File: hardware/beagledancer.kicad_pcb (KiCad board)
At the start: 2 copper layers, 32 x 23.1 mm, 12 parts, among them J1 USB-MICRO-B, P9 BeagleBone, U1 MAX3421, X1 XTAL4PIN

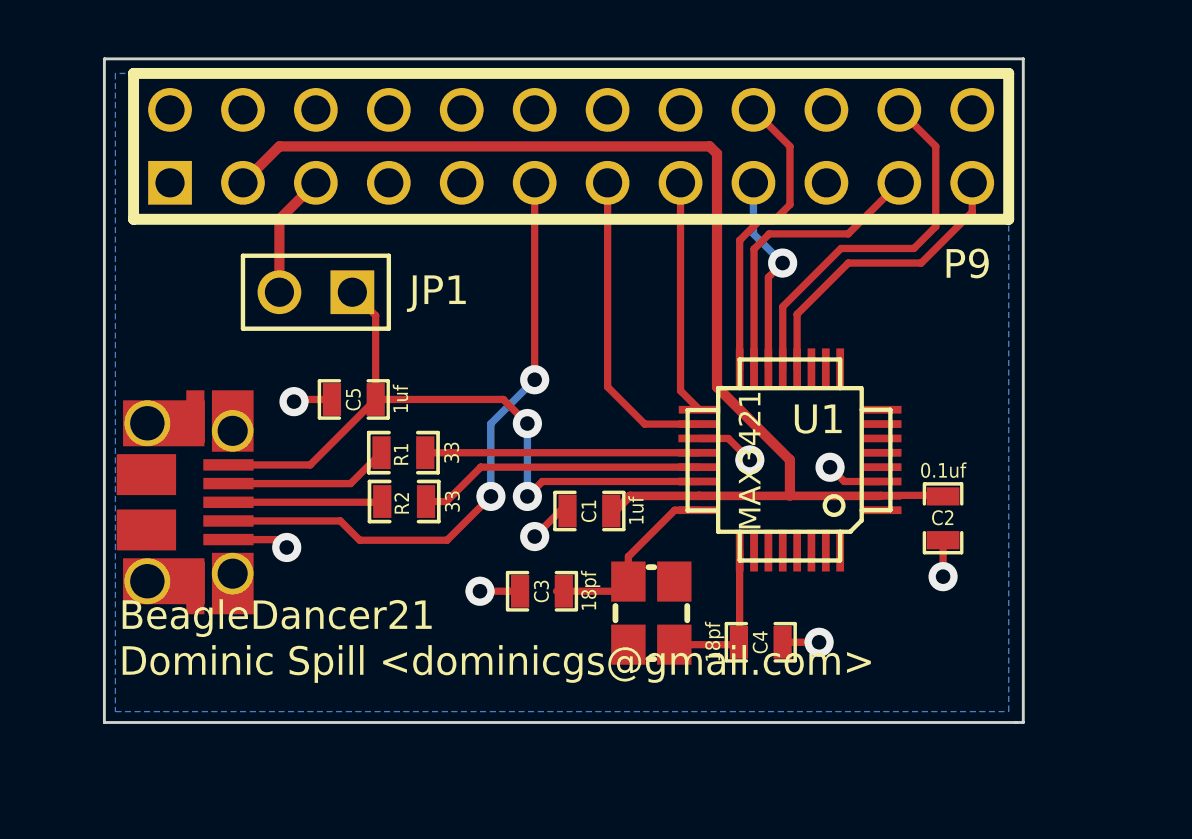
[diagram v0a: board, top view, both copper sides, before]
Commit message: Change crystal to match FaceDancer
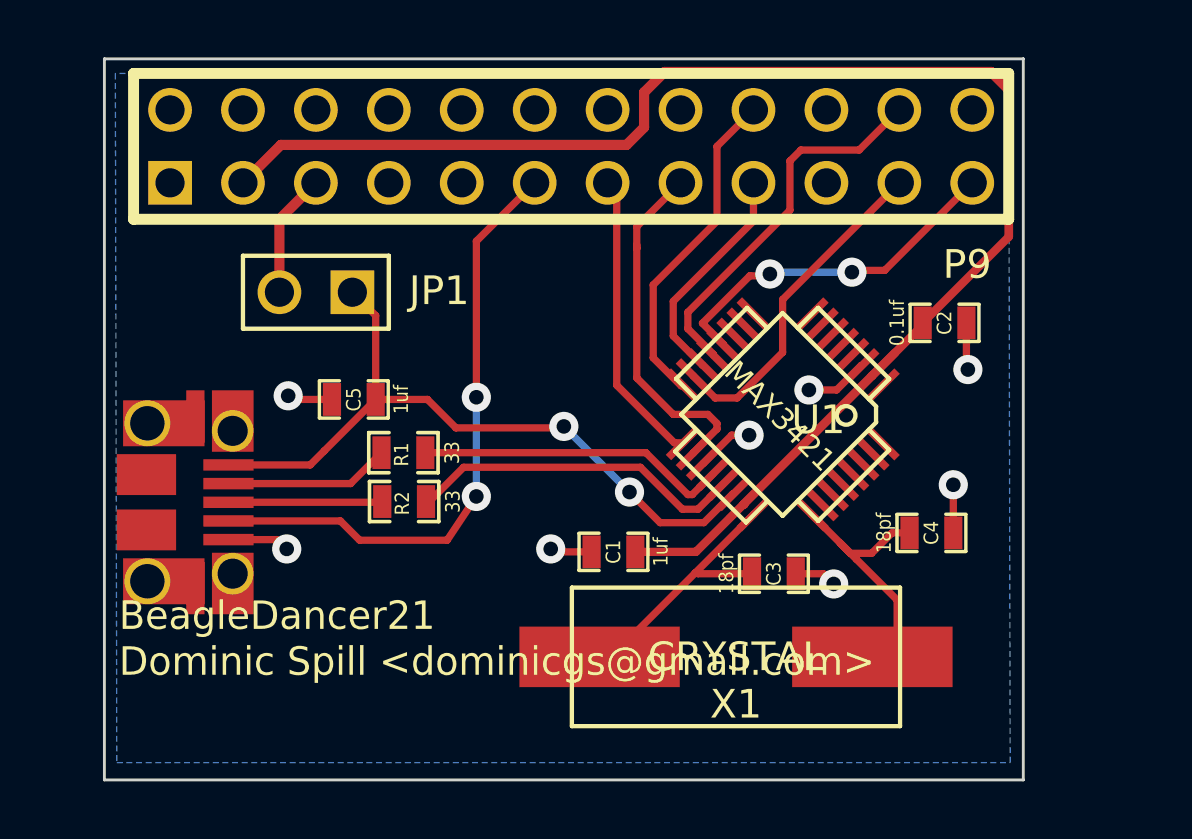
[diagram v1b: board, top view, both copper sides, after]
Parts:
- X1: value XTAL4PIN -> CRYSTAL; footprint GSG-XTAL3.2x2.5mm -> HC49-US
- moved C3 8.10 mm to (221.7, 154.6), turned to 0 degrees
- moved C4 7.06 mm to (227.2, 153.2)
- moved C2 6.81 mm to (227.6, 145.8), turned to 0 degrees
- moved X1 3.32 mm to (220.4, 157.5), turned to 0 degrees
- moved C1 1.65 mm to (216.1, 153.8)
- moved U1 1.61 mm to (222.0, 149.0), turned to 135 degrees
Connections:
- P9 pad 13: INT -> GPX
- P9 pad 15: GPX -> INT
- X1 pad 2: N-0000021 (its old number) -> /XO
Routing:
- net +3.3V: track 41.8 -> 53.2 mm
- net /D-: track 19.0 -> 11.0 mm
- net SPI0_D1: track 17.2 -> 11.5 mm
- net /XI: track 13.5 -> 8.28 mm
- net SPI0_D0: track 14.2 -> 11.7 mm
- net GPX: track 8.18 -> 10.7 mm
- net SPI0_CS0: track 10.8 -> 8.60 mm, vias 1 -> 0
- net SPI0_SCLK: track 15.3 -> 13.2 mm
- net /D+: track 10.0 -> 11.8 mm
- net INT: track 11.2 -> 12.8 mm
- net GND: track 13.1 -> 14.5 mm
- net /RES: track 12.3 -> 12.5 mm, vias 0 -> 2
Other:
- board size 32 x 23.1 mm -> 32 x 25.1 mm
- net class Power: trace_width 0.3556 -> 0.29
- board text added: "github.com/dominicgs/BeagleDancer"
- board text removed: "https://github.com/dominicgs/BeagleDancer"

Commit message: Some minor tweaks to make everything fit properly.
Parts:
- moved C1 12.5 mm to (227.9, 149.7), turned to 270 degrees
- moved C3 5.14 mm to (216.6, 153.8), turned to 180 degrees
- moved C4 0.48 mm to (226.9, 153.6)
- moved X1 0.42 mm to (220.8, 157.4)
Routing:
- net /XO: track 8.37 -> 7.26 mm
